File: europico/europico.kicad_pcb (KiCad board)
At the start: 2 copper layers, 5 parts, among them J1 Left, J2 Right, J3 SWD, J4 USB_B_Mini, J5 BOOTSEL

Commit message: Update
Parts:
- removed J5: BOOTSEL, Connector_PinHeader_2.54mm:PinHeader_1x01_P2.54mm_Vertical
- J2: value Right -> Conn_01x21_Male; footprint Connector_PinHeader_2.54mm:PinHeader_1x20_P2.54mm_Vertical -> Connector_PinHeader_2.54mm:PinHeader_1x21_P2.54mm_Vertical
- moved J2 2.81 mm to (101.6, 71.1)
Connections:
- net Net-(J1-Pad1) renamed /GPIO0
- net Net-(J1-Pad10) renamed /GPIO7
- net Net-(J1-Pad11) renamed /GPIO8
- net Net-(J1-Pad12) renamed /GPIO9
- net Net-(J1-Pad14) renamed /GPIO10
- net Net-(J1-Pad15) renamed /GPIO11
- net Net-(J1-Pad16) renamed /GPIO12
- net Net-(J1-Pad17) renamed /GPIO13
- net Net-(J1-Pad19) renamed /GPIO14
- net Net-(J1-Pad2) renamed /GPIO1
- net Net-(J1-Pad20) renamed /GPIO15
- net Net-(J1-Pad4) renamed /GPIO2
- net Net-(J1-Pad5) renamed /GPIO3
- net Net-(J1-Pad6) renamed /GPIO4
- net Net-(J1-Pad7) renamed /GPIO5
- net Net-(J1-Pad9) renamed /GPIO6
- net Net-(J2-Pad10) renamed /GPIO27_ADC1
- net Net-(J2-Pad11) renamed /GPIO26_ADC0
- net Net-(J2-Pad12) renamed /RUN
- net Net-(J2-Pad15) renamed /GPIO21
- net Net-(J2-Pad16) renamed /GPIO20
- net Net-(J2-Pad17) renamed /GPIO19
- net Net-(J2-Pad20) renamed /GPIO17
- net Net-(J2-Pad5) renamed /3V3_EN
- net Net-(J2-Pad6) renamed /3V3
- net Net-(J2-Pad7) renamed /ADC_VREF
- net Net-(J4-Pad2) renamed /USB_D-
- net Net-(J4-Pad3) renamed /USB_D+
- J2 pad 1: Net-(J2-Pad1) -> /BOOTSEL
- J2 pad 13: GND -> /GPIO22
- J2 pad 14: Net-(J2-Pad14) -> GND
- J2 pad 18: GND -> /GPIO18
- J2 pad 19: Net-(J2-Pad19) -> GND
- J2 pad 2: Net-(J2-Pad2) -> /VBUS
- J2 pad 3: GND -> /VSYS
- J2 pad 4: Net-(J2-Pad4) -> GND
- J2 pad 8: GND -> /GPIO28_ADC2
- J2 pad 9: Net-(J2-Pad9) -> GND
- J4 pad 1: Net-(J2-Pad1) -> /VBUS
- J4 pad 6: GND -> unconnected-(J4-Pad6)

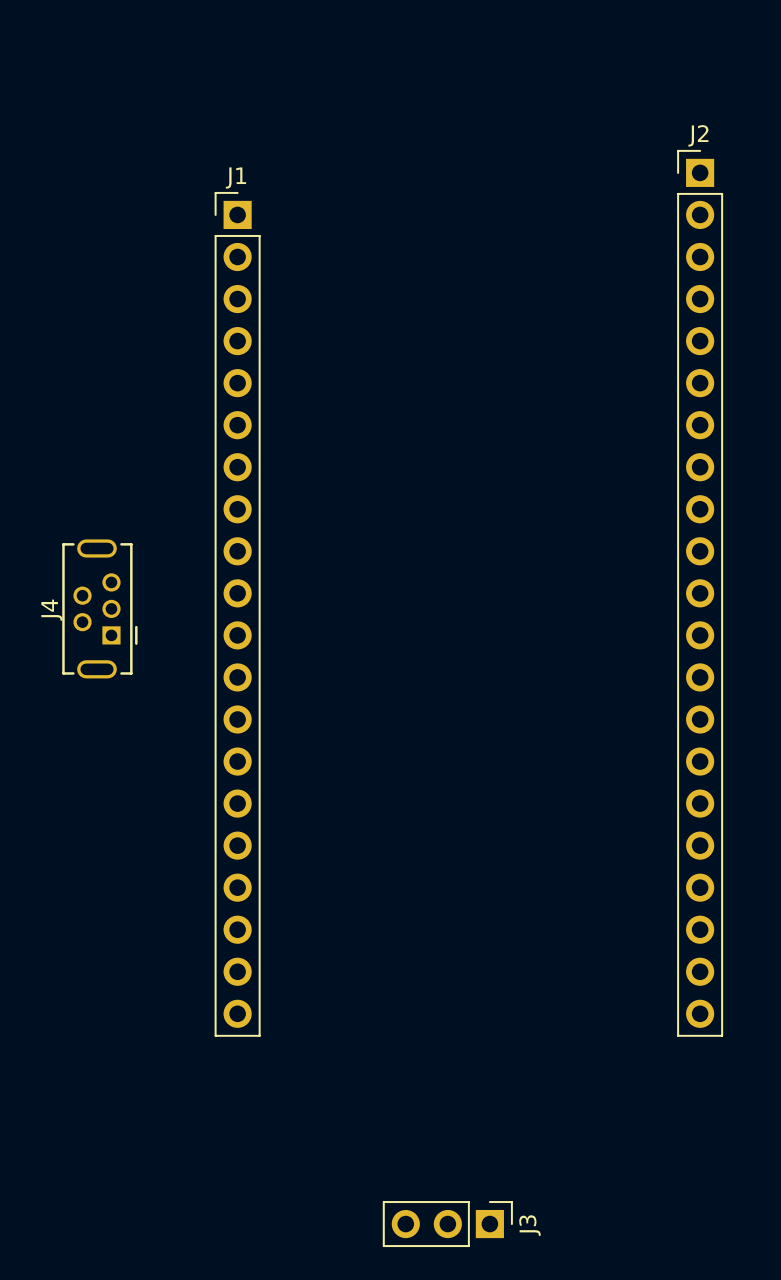
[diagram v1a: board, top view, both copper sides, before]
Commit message: basic Pico footprint
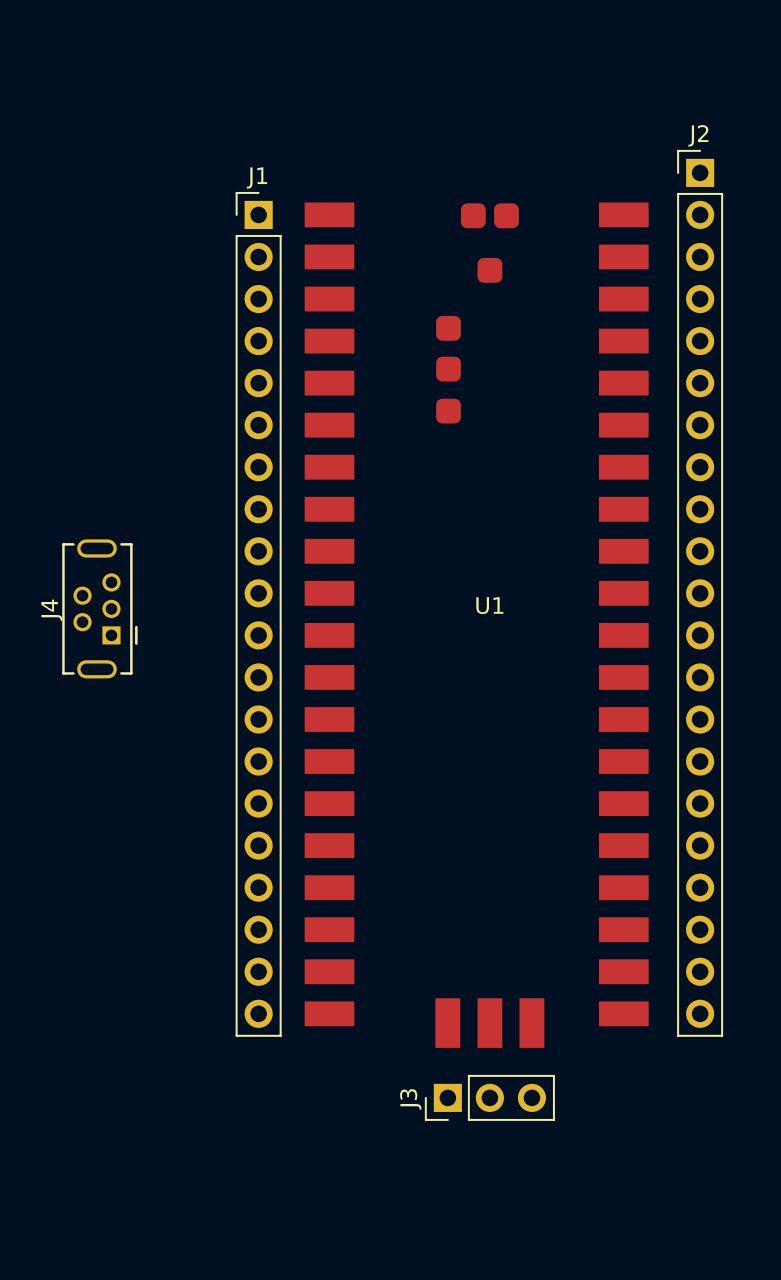
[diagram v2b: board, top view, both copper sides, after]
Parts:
- added U1: Pico, Pico:Pico, F.Cu at (88.9, 97.8)
- J1: value Left -> Conn_01x20_Male
- J3: value SWD -> Conn_01x03_Male
- J4: value USB_B_Mini -> MUSBB15134
- moved J3 8.03 mm to (86.4, 127.0), turned to 90 degrees
- moved J1 1.27 mm to (74.9, 73.7)

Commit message: Updates
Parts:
- moved J4 3.59 mm to (68.6, 101.6)
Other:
- board outline added: 40.6 x 61 mm
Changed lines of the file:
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@@
   (net 42 "unconnected-(U1-Pad48)")
   (footprint "Connector_USB:USB_Mini-B_Tensility_54-00023_Vertical" (layer "F.Cu")
-    (at 66.04 99.06 90)
+    (at 68.58 101.6 90)
     (descr "http://www.tensility.com/pdffiles/54-00023.pdf")
     (tags "usb mini receptacle vertical")
@@
     )
   )
+  (gr_rect (start 104.14 68.58) (end 63.5 129.54) (layer "Edge.Cuts") (width 0.1) (fill none))
 )

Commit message: USB connector, hell yea
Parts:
- J4: footprint Connector_USB:USB_Mini-B_Tensility_54-00023_Vertical -> USB:AMPHENOL_MUSBB15134
- moved J4 2.54 mm to (68.6, 99.1), turned to -90 degrees
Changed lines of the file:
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@@
   (net 38 "/USB_D-")
   (net 39 "/USB_D+")
-  (net 40 "unconnected-(J4-Pad6)")
-  (net 41 "unconnected-(U1-Pad47)")
-  (net 42 "unconnected-(U1-Pad48)")
-  (footprint "Connector_USB:USB_Mini-B_Tensility_54-00023_Vertical" (layer "F.Cu")
-    (at 68.58 101.6 90)
-    (descr "http://www.tensility.com/pdffiles/54-00023.pdf")
-    (tags "usb mini receptacle vertical")
-    (property "Sheetfile" "europico.kicad_sch")
-    (property "Sheetname" "")
-    (attr through_hole)
-    (fp_text reference "J4" (at 1.6 -3.7 90) (layer "F.SilkS")
-      (effects (font (size 1 1) (thickness 0.15)))
-    )
-    (fp_text value "MUSBB15134" (at 1.5 2.2 90) (layer "F.Fab")
-      (effects (font (size 1 1) (thickness 0.15)))
-    )
-    (fp_text user "${REFERENCE}" (at 1.5 -1 90) (layer "F.Fab")
-      (effects (font (size 1 1) (thickness 0.15)))
-    )
-    (fp_line (start 5.5 -2.9) (end 5.5 -2.3) (layer "F.SilkS") (width 0.15))
-    (fp_line (start -2.3 -2.9) (end 5.5 -2.9) (layer "F.SilkS") (width 0.15))
-    (fp_line (start 5.5 1.2) (end 5.5 0.6) (layer "F.SilkS") (width 0.15))
-    (fp_line (start -0.5 1.5) (end 0.5 1.5) (layer "F.SilkS") (width 0.15))
-    (fp_line (start -2.3 0.6) (end -2.3 1.2) (layer "F.SilkS") (width 0.15))
-    (fp_line (start -2.3 -2.3) (end -2.3 -2.9) (layer "F.SilkS") (width 0.15))
-    (fp_line (start -2.3 1.2) (end 5.5 1.2) (layer "F.SilkS") (width 0.15))
-    (fp_line (start 6 -3.2) (end -2.8 -3.2) (layer "F.CrtYd") (width 0.05))
-    (fp_line (start -2.8 1.5) (end 6 1.5) (layer "F.CrtYd") (width 0.05))
-    (fp_line (start -2.8 -3.2) (end -2.8 1.5) (layer "F.CrtYd") (width 0.05))
-    (fp_line (start 6 1.5) (end 6 -3.2) (layer "F.CrtYd") (width 0.05))
-    (fp_line (start 5.2 -2.6) (end 5.2 0.9) (layer "F.Fab") (width 0.15))
-    (fp_line (start 5.2 -2.6) (end -2 -2.6) (layer "F.Fab") (width 0.15))
-    (fp_line (start -2 0.9) (end -2 -2.6) (layer "F.Fab") (width 0.15))
-    (fp_line (start 0.7 0.9) (end 5.2 0.9) (layer "F.Fab") (width 0.15))
-    (fp_line (start 0 0.2) (end 0.7 0.9) (layer "F.Fab") (width 0.15))
-    (fp_line (start -2 0.9) (end -0.7 0.9) (layer "F.Fab") (width 0.15))
-    (fp_line (start -0.7 0.9) (end 0 0.2) (layer "F.Fab") (width 0.15))
-    (pad "1" thru_hole rect (at 0 0 90) (size 1.1 1.1) (drill 0.7) (layers *.Cu *.Mask)
-      (net 22 "/VBUS") (pinfunction "VBUS") (pintype "power_out"))
-    (pad "2" thru_hole circle (at 0.8 -1.75 90) (size 1.1 1.1) (drill 0.7) (layers *.Cu *.Mask)
-      (net 38 "/USB_D-") (pinfunction "D-") (pintype "bidirectional"))
-    (pad "3" thru_hole circle (at 1.6 0 90) (size 1.1 1.1) (drill 0.7) (layers *.Cu *.Mask)
-      (net 39 "/USB_D+") (pinfunction "D+") (pintype "bidirectional"))
-    (pad "4" thru_hole circle (at 2.4 -1.75 90) (size 1.1 1.1) (drill 0.7) (layers *.Cu *.Mask)
-      (net 4 "unconnected-(J4-Pad4)") (pinfunction "ID") (pintype "passive+no_connect"))
-    (pad "5" thru_hole circle (at 3.2 0 90) (size 1.1 1.1) (drill 0.7) (layers *.Cu *.Mask)
-      (net 1 "GND") (pinfunction "GND") (pintype "power_out"))
-    (pad "6" thru_hole oval (at 5.25 -0.875 90) (size 1.1 2.4) (drill oval 0.7 2) (layers *.Cu *.Mask)
-      (net 40 "unconnected-(J4-Pad6)") (pinfunction "Shield") (pintype "passive+no_connect"))
-    (pad "6" thru_hole oval (at -2.05 -0.875 90) (size 1.1 2.4) (drill oval 0.7 2) (layers *.Cu *.Mask)
-      (net 40 "unconnected-(J4-Pad6)") (pinfunction "Shield") (pintype "passive+no_connect"))
-    (model "${KICAD6_3DMODEL_DIR}/Connector_USB.3dshapes/USB_Mini-B_Tensility_54-00023_Vertical.wrl"
-      (offset (xyz 0 0 0))
-      (scale (xyz 1 1 1))
-      (rotate (xyz 0 0 0))
-    )
-  )
+  (net 40 "unconnected-(U1-Pad47)")
+  (net 41 "unconnected-(U1-Pad48)")
+  (net 42 "unconnected-(J4-PadS1)")
   (footprint "Pico:Pico" (layer "F.Cu")
     (at 88.9 97.79)
@@
       (net 39 "/USB_D+") (pinfunction "TP3") (pintype "bidirectional"))
     (pad "47" smd roundrect (at -2.5 -17.28) (size 1.5 1.5) (layers "F.Cu" "F.Paste" "F.Mask") (roundrect_rratio 0.25)
-      (net 41 "unconnected-(U1-Pad47)") (pinfunction "TP4") (pintype "bidirectional+no_connect"))
+      (net 40 "unconnected-(U1-Pad47)") (pinfunction "TP4") (pintype "bidirectional+no_connect"))
     (pad "48" smd roundrect (at -2.5 -14.82) (size 1.5 1.5) (layers "F.Cu" "F.Paste" "F.Mask") (roundrect_rratio 0.25)
-      (net 42 "unconnected-(U1-Pad48)") (pinfunction "TP5") (pintype "bidirectional+no_connect"))
+      (net 41 "unconnected-(U1-Pad48)") (pinfunction "TP5") (pintype "bidirectional+no_connect"))
     (pad "49" smd roundrect (at -2.5 -12.28) (size 1.5 1.5) (layers "F.Cu" "F.Paste" "F.Mask") (roundrect_rratio 0.25)
       (net 21 "/BOOTSEL") (pinfunction "TP6") (pintype "input"))
@@
     )
   )
+  (footprint "USB:AMPHENOL_MUSBB15134" (layer "F.Cu")
+    (at 68.58 99.06 -90)
+    (property "MANUFACTURER" "Amphenol")
+    (property "MAXIMUM_PACKAGE_HEIGHT" "10.25 mm")
+    (property "PARTREV" "K")
+    (property "STANDARD" "Manufacturer Recommendations")
+    (property "Sheetfile" "europico.kicad_sch")
+    (property "Sheetname" "")
+    (attr through_hole)
+    (fp_text reference "J4" (at -6.325 -4.635 90) (layer "F.SilkS")
+      (effects (font (size 1 1) (thickness 0.15)))
+    )
+    (fp_text value "MUSBB15134" (at 2.565 -3.135 90) (layer "F.Fab")
+      (effects (font (size 1 1) (thickness 0.15)))
+    )
+    (fp_text user "PCB EDGE" (at 10.6 3.6 90) (layer "F.Fab")
+      (effects (font (size 0.48 0.48) (thickness 0.15)))
+    )
+    (fp_line (start -9.5 3.78) (end -9.5 -1.33) (layer "F.SilkS") (width 0.127))
+    (fp_line (start -9.5 -1.33) (end -5.5 -1.33) (layer "F.SilkS") (width 0.127))
+    (fp_line (start -9.5 3.78) (end 9.5 3.78) (layer "F.SilkS") (width 0.127))
+    (fp_line (start 9.5 -1.33) (end 5.5 -1.33) (layer "F.SilkS") (width 0.127))
+    (fp_line (start 9.5 3.78) (end 9.5 -1.33) (layer "F.SilkS") (width 0.127))
+    (fp_circle (center -1.6 -2.4) (end -1.5 -2.4) (layer "F.SilkS") (width 0.2) (fill none))
+    (fp_line (start 4.85 9.2) (end -4.85 9.2) (layer "F.CrtYd") (width 0.05))
+    (fp_line (start 10.25 -2.05) (end 10.25 6.7) (layer "F.CrtYd") (width 0.05))
+    (fp_line (start -4.85 6.7) (end -10.25 6.7) (layer "F.CrtYd") (width 0.05))
+    (fp_line (start -4.85 9.2) (end -4.85 6.7) (layer "F.CrtYd") (width 0.05))
+    (fp_line (start 10.25 6.7) (end 4.85 6.7) (layer "F.CrtYd") (width 0.05))
+    (fp_line (start -10.25 6.7) (end -10.25 -2.05) (layer "F.CrtYd") (width 0.05))
+    (fp_line (start 4.85 6.7) (end 4.85 9.2) (layer "F.CrtYd") (width 0.05))
+    (fp_line (start -10.25 -2.05) (end 10.25 -2.05) (layer "F.CrtYd") (width 0.05))
+    (fp_line (start -10 4.25) (end -10 6.45) (layer "F.Fab") (width 0.127))
+    (fp_line (start -4.6 6.45) (end -4.6 8.95) (layer "F.Fab") (width 0.127))
+    (fp_line (start 10 4.25) (end 9.5 4.25) (layer "F.Fab") (width 0.127))
+    (fp_line (start -11 3.78) (end 11 3.78) (layer "F.Fab") (width 0.127))
+    (fp_line (start -4.6 6.45) (end 4.6 6.45) (layer "F.Fab") (width 0.127))
+    (fp_line (start -9.5 4.25) (end -10 4.25) (layer "F.Fab") (width 0.127))
+    (fp_line (start -10 6.45) (end -4.6 6.45) (layer "F.Fab") (width 0.127))
+    (fp_line (start 4.6 8.95) (end 4.6 6.45) (layer "F.Fab") (width 0.127))
+    (fp_line (start 9.5 4.25) (end -9.5 4.25) (layer "F.Fab") (width 0.127))
+    (fp_line (start 9.5 -1.33) (end 9.5 4.25) (layer "F.Fab") (width 0.127))
+    (fp_line (start -9.5 -1.33) (end 9.5 -1.33) (layer "F.Fab") (width 0.127))
+    (fp_line (start -4.6 8.95) (end 4.6 8.95) (layer "F.Fab") (width 0.127))
+    (fp_line (start -9.5 4.25) (end -9.5 -1.33) (layer "F.Fab") (width 0.127))
+    (fp_line (start 10 6.45) (end 10 4.25) (layer "F.Fab") (width 0.127))
+    (fp_line (start 4.6 6.45) (end 10 6.45) (layer "F.Fab") (width 0.127))
+    (fp_circle (center -1.6 -2.4) (end -1.5 -2.4) (layer "F.Fab") (width 0.2) (fill none))
+    (pad "1" thru_hole circle (at -1.6 -0.6 270) (size 1.258 1.258) (drill 0.75) (layers *.Cu *.Mask)
+      (net 22 "/VBUS") (pinfunction "VCC") (pintype "power_in"))
+    (pad "2" thru_hole circle (at -0.8 0.6 270) (size 1.258 1.258) (drill 0.75) (layers *.Cu *.Mask)
+      (net 38 "/USB_D-") (pinfunction "D-") (pintype "bidirectional"))
+    (pad "3" thru_hole circle (at 0 -0.6 270) (size 1.258 1.258) (drill 0.75) (layers *.Cu *.Mask)
+      (net 39 "/USB_D+") (pinfunction "D+") (pintype "bidirectional"))
+    (pad "4" thru_hole circle (at 0.8 0.6 270) (size 1.258 1.258) (drill 0.75) (layers *.Cu *.Mask)
+      (net 4 "unconnected-(J4-Pad4)") (pinfunction "ID") (pintype "bidirectional+no_connect"))
+    (pad "5" thru_hole circle (at 1.6 -0.6 270) (size 1.258 1.258) (drill 0.75) (layers *.Cu *.Mask)
+      (net 1 "GND") (pinfunction "GND") (pintype "power_in"))
+    (pad "S1" thru_hole oval (at -4.25 0 270) (size 1.8 3.6) (drill oval 1.03 3.15) (layers *.Cu *.Mask)
+      (net 42 "unconnected-(J4-PadS1)") (pinfunction "SHIELD") (pintype "passive+no_connect"))
+    (pad "S2" thru_hole oval (at 4.25 0 270) (size 1.8 3.6) (drill oval 1.03 3.15) (layers *.Cu *.Mask)
+      (net 42 "unconnected-(J4-PadS1)") (pinfunction "SHIELD") (pintype "passive+no_connect"))
+  )
   (footprint "Connector_PinHeader_2.54mm:PinHeader_1x21_P2.54mm_Vertical" (layer "F.Cu")
     (at 101.6 71.12)
@@
     (property "Sheetname" "")
     (attr through_hole)
-    (fp_text reference "J2" (at 0 -2.33) (layer "F.SilkS")
-      (effects (font (size 1 1) (thickness 0.15)))
-    )
+    (fp_text reference "J2" (at -2.54 0) (layer "F.SilkS")
+      (effects (font (size 1 1) (thickness 0.15)))
+    )

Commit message: WIP
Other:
- board size 40.6 x 61 mm -> 42 x 63.2 mm
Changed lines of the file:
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@@
     )
   )
-  (gr_rect (start 104.14 68.58) (end 63.5 129.54) (layer "Edge.Cuts") (width 0.1) (fill none))
+  (gr_line (start 62.4586 66.3956) (end 62.4586 87.4268) (layer "Edge.Cuts") (width 0.1))
+  (gr_line (start 64.7954 87.4014) (end 64.7446 112.2172) (layer "Edge.Cuts") (width 0.1))
+  (gr_line (start 62.4586 112.268) (end 62.4586 129.5908) (layer "Edge.Cuts") (width 0.1))
+  (gr_line (start 62.5094 87.4268) (end 64.7954 87.4014) (layer "Edge.Cuts") (width 0.1))
+  (gr_line (start 62.4586 129.5908) (end 104.4448 129.6162) (layer "Edge.Cuts") (width 0.1))
+  (gr_line (start 104.4448 66.3956) (end 104.4448 129.6162) (layer "Edge.Cuts") (width 0.1))
+  (gr_line (start 104.4448 66.3956) (end 62.4586 66.3956) (layer "Edge.Cuts") (width 0.1))
+  (gr_line (start 64.7446 112.2172) (end 62.4586 112.2172) (layer "Edge.Cuts") (width 0.1))
 )
